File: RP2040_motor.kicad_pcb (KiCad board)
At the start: 4 copper layers, 98.7 x 71.3 mm, 246 parts, among them J1 USB_C_Receptacle_USB2.0, J10 Conn_01x03, J11 Conn_01x04, J12 Conn_01x06, J13 Conn_01x03, J14 Conn_01x03, J15 Conn_01x05, J2 Conn_01x04, J3 Conn_01x05, J4 Conn_01x05, J5 Conn_01x06, J6 USB_C_Receptacle_USB2.0, J7 Conn_01x02, J8 RJ45, J9 Conn_01x03, M1A1 HIGHCURRENTPAD2, M1B1 HIGHCURRENTPAD2, M1C1 HIGHCURRENTPAD2, M2A1 HIGHCURRENTPAD2, M2B1 HIGHCURRENTPAD2, M2C1 HIGHCURRENTPAD2, SW1 SW_MEC_5G, SW2 SW_MEC_5G, U1 EG2131, U10 LD1086DT33TR, U11 XL7045, U12 W25Q16JVSSIQ, U13 W25Q16JVSSIQ, U14 CC6920B, U15 RP2040, U16 ADC081S021CISD/NOPB, U17 isolator, U18 MCP2515-xSO, U19 RP2040, U2 EG2131, U20 CC6920B, U21 EL357N(C)(TA)-G, U22 CC6920B, U3 CC6920B, U4 EG2131, U5 EG2131, U7 EG2131, U8 EG2131, U9 ADC081S021CISD/NOPB, Y1 Crystal_GND24, Y2 Crystal_GND24, Y3 Crystal_GND24

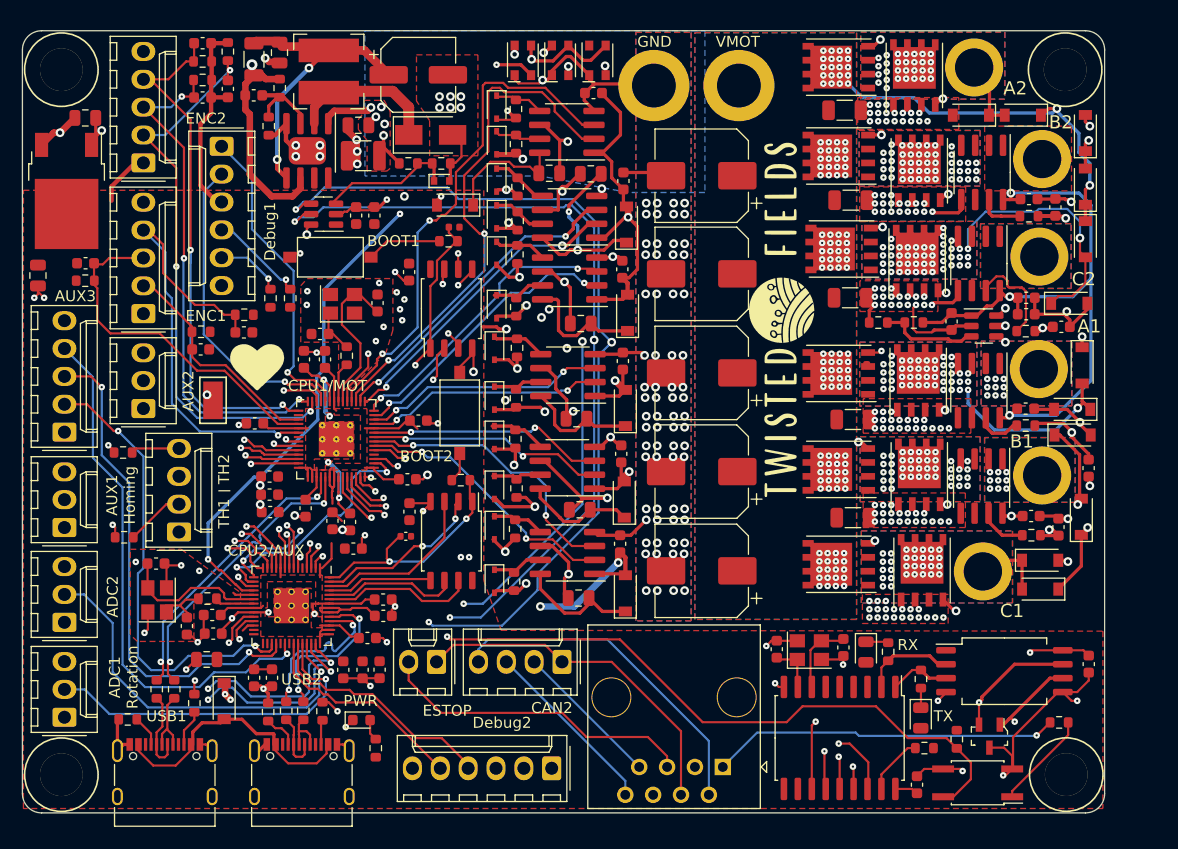
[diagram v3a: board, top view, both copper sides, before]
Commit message: Updated design with Dual CPUs and improved current measurement
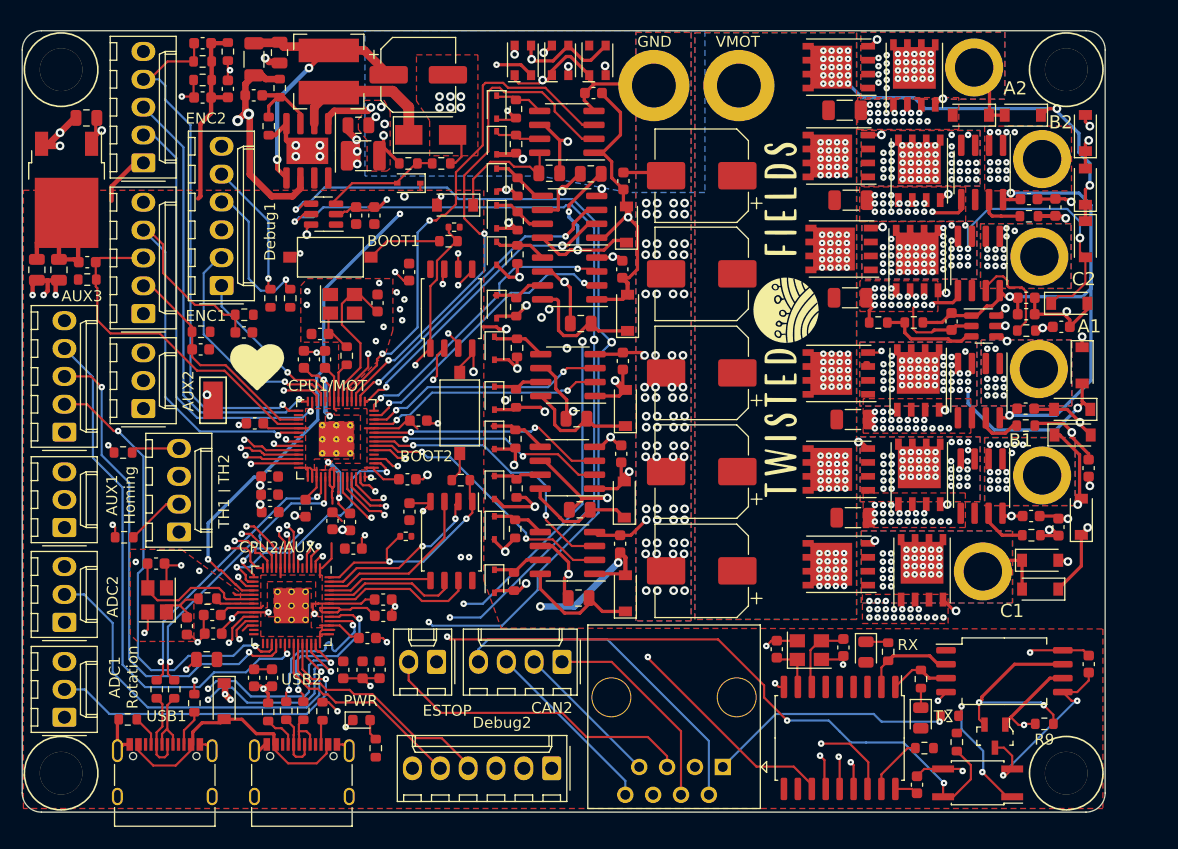
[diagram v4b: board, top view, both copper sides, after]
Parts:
- removed D36: DNS, Diode_SMD:D_SOD-523
- added C81: 10u, Capacitor_SMD:C_0805_2012Metric, F.Cu at (66.1, 89.8)
- added D31: 1N4148WS, Diode_SMD:D_SOD-323, F.Cu at (98.0, 81.9)
- added R9: 487, Resistor_SMD:R_0603_1608Metric, F.Cu at (155.9, 131.2)
- C55, C59, C65, C66, C67, C68, C69, C70, R39, R59: value 0.1uF -> 100n
- C71: value 0.1uF -> 47nF
- R42, R51: footprint Capacitor_SMD:C_0402_1005Metric -> Resistor_SMD:R_0402_1005Metric
- U11: footprint RP2040_minimal:SOIC-8_3.9x4.9mm_P1.27mm_POWERPAD -> Package_SO:SOIC-8-1EP_3.9x4.9mm_P1.27mm_EP2.41x3.81mm
- moved J5 12.7 mm to (80.9, 91.2), turned to 90 degrees
- moved R75 10.0 mm to (147.3, 130.5)
- moved C22 0.53 mm to (64.1, 89.8)
- moved D40 0.50 mm to (151.4, 132.3)
- moved G*** 0.40 mm to (132.4, 93.3)
- moved R76 0.25 mm to (148.0, 132.9)
- moved R56 0.21 mm to (68.7, 90.7)
- moved C61 0.18 mm to (68.7, 89.1)
- moved H3 0.14 mm to (66.3, 135.7)
- moved H1 0.13 mm to (157.9, 135.7)
- moved U10 0.10 mm to (66.8, 82.5)
- moved C20 0.10 mm to (68.6, 76.0)
- moved H2 0.10 mm to (157.9, 71.5)
- moved R1 0.07 mm to (154.3, 95.3)
- renumbered C$7 to C72, U$1 to C73, C$6 to C74, C$5 to C75, C$8 to C76, C$1 to C77, C$2 to C78, C$3 to C79, C$4 to C80
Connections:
- U11 pad 7: (no net) -> unconnected-(U11-Pad7)
- U11 pad 8: (no net) -> unconnected-(U11-Pad8)
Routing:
- net +3V3: track 236.6 -> 253.3 mm
- net SWCLK: track 28.6 -> 15.5 mm
- net ESTOP_SQUARE: track 31.8 -> 22.6 mm
- net CANH0: track 39.6 -> 48.5 mm, vias 1 -> 2
- net SWD: track 29.0 -> 21.5 mm
- net TXO: track 33.8 -> 40.0 mm
- net RXI: track 35.7 -> 40.6 mm
- net SPI1_INT: track 60.6 -> 56.8 mm
- net Net-(R75-Pad2): track 8.89 -> 11.5 mm, vias 0 -> 2
- net GND: track 191.6 -> 193.9 mm, vias 251 -> 252
- net SPI1_TX_2: track 76.7 -> 74.4 mm
- net SPI1_SCK_2: track 78.7 -> 76.5 mm
- net CANL0: track 44.3 -> 46.4 mm
- net Net-(D31-Pad2): track 12.3 -> 10.8 mm
- net M2B: track 52.8 -> 54.0 mm, vias 50 -> 52
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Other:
- board size 98.7 x 71.3 mm -> 98.8 x 71.2 mm
- rule pad_to_mask_clearance: 0.051 -> 0
- board text added: "Many thanks to Daniel Theobald and our supporters on open collective for funding this work!"
- board text removed: "Funded By Daniel Theobald Thanks Daniel!"
